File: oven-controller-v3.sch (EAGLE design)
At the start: 48 parts, among them Q1 IRFL310, Q2 IRFL310, Q3 IRFL310, Q4 IRFL310, U1 ARDUINO_SHIELDLONGPADS, U2 MAX31855, U3 MAX31855, U4 MAX31855, U5 MAX31855, U6 MAX31855, U7 SN74LVC1G139

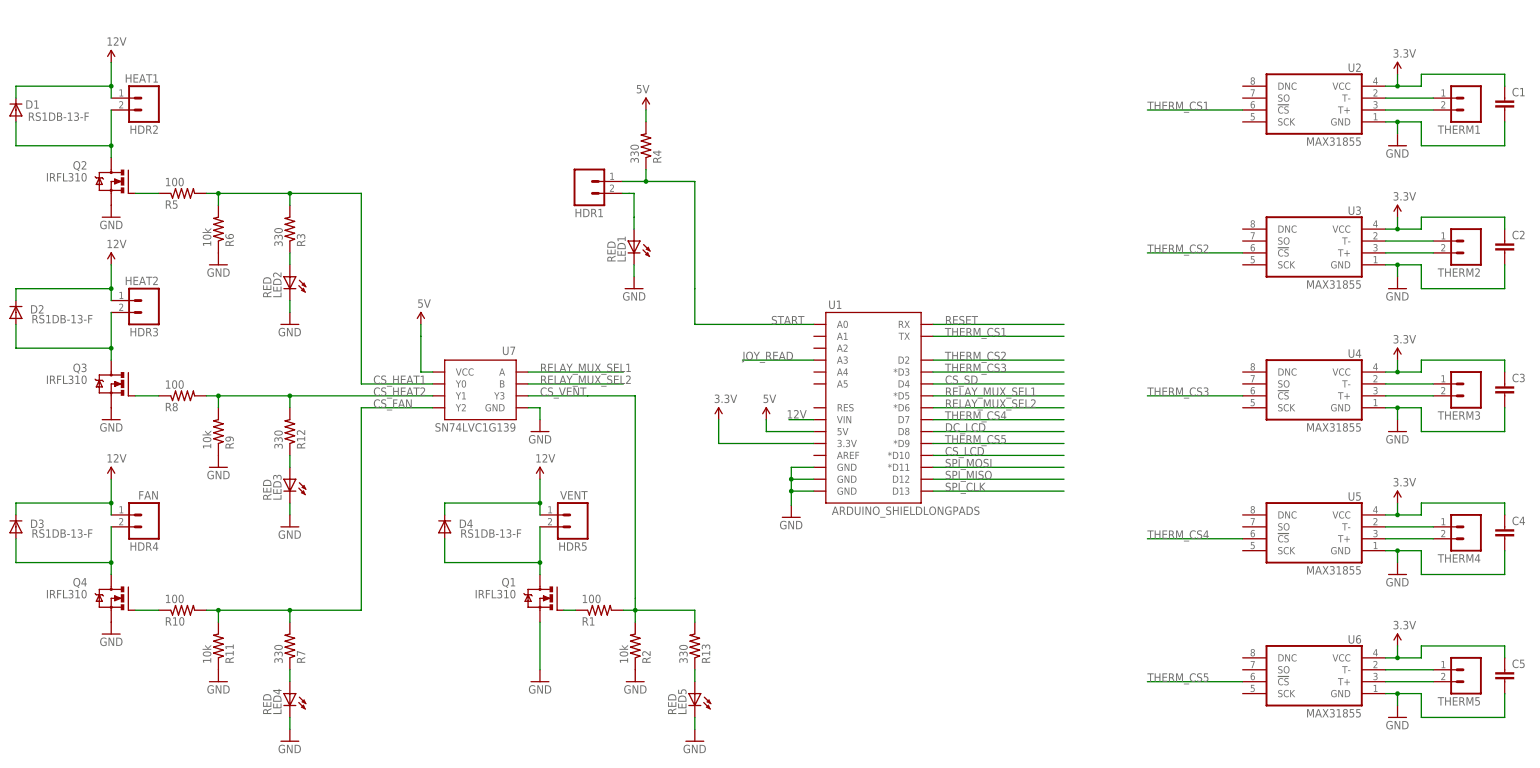
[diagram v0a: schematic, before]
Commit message: Removed diodes. FETs now SOT23-3. Schematic and layout done. Ready for review.
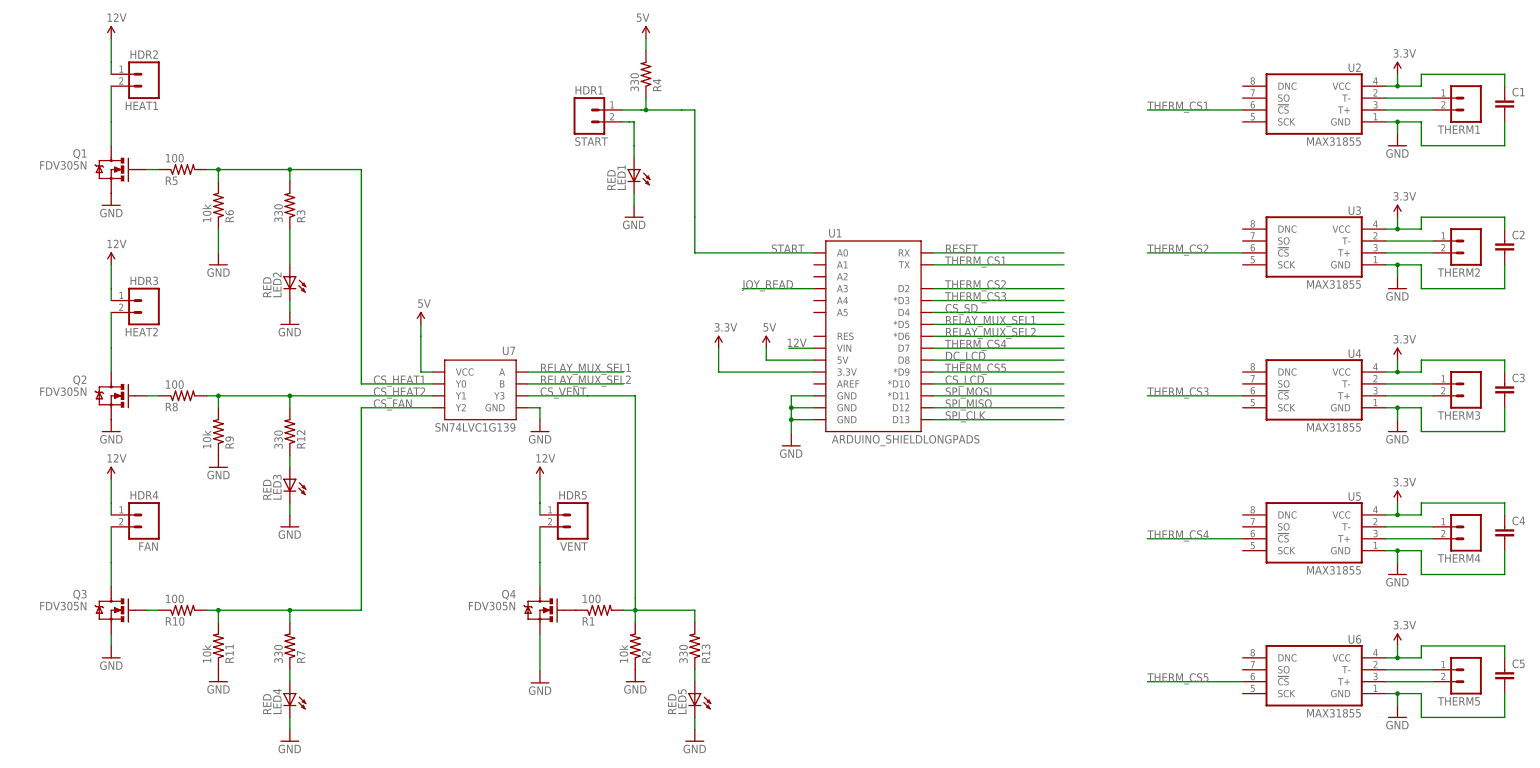
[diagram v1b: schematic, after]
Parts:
- removed D1, D2, D3, D4: RS1DB-13-F, SparkFun-DiscreteSemi:DIODESMA-ALT
- removed HDR1: (no value), SparkFun-Connectors:M023.5MM_LOCK
- removed HDR2: HEAT1, SparkFun-Connectors:M023.5MM_LOCK
- added HEAT1: HDR2, SparkFun-Connectors:M023.5MM_LOCK
- added START: HDR1, SparkFun-Connectors:M023.5MM_LOCK
- FAN: value FAN -> HDR4
- HEAT2: value HEAT2 -> HDR3
- Q1, Q2, Q3, Q4: value IRFL310 -> FDV305N; device transistor-power:IRF520 -> SparkFun-DiscreteSemi:MOSFET-NCHANNELSMD
- VENT: value VENT -> HDR5
- renumbered HDR3 to HEAT2, HDR4 to FAN, HDR5 to VENT
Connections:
- net 12V: now also HEAT1.1; no longer D1.C, D2.C, D3.C, D4.C, HDR2.1
- net HDR3: now also Q3.D; no longer D3.A, Q4.D
- net N$1: now also Q1.G; no longer Q2.G
- net N$10: now also START.2; no longer HDR1.2
- net N$2: now also Q4.G; no longer Q1.G
- net N$20: now also Q2.G; no longer Q3.G
- net N$21: now also Q2.D; no longer D2.A, Q3.D
- net N$23: now also Q3.G; no longer Q4.G
- net N$3: now also Q4.D; no longer D4.A, Q1.D
- net N$4: now also HEAT1.2, Q1.D; no longer D1.A, HDR2.2, Q2.D
- net START: now also START.1; no longer HDR1.1
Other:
- moved on the sheet: LED1, R3, R4, R5, R6, U1
